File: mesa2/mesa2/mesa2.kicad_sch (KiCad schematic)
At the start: 49 parts, among them J2 Tag-Connect TC2030

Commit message: Record the Rev B design review
The board passes: DRC has no errors, schematic parity is clean, the
outline closes through the Tiny2040 cutout, all 36 footprints still sit
where revb-placement.json puts them, and the silkscreen carries the rev.

Correct the GPIO map in LAYOUT.md, which still claimed the columns ran
GP4 up to GP7. They run GP7 down to GP4 now, reassigned after the
columns paired by finger, and the firmware reads that table.

Assisted-by: Claude:opus-5
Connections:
- net COL_1: now also A1.7 (GP7); no longer A1.4 (GP4)
- net COL_2: now also A1.6 (GP6); no longer A1.5 (GP5)
- net COL_3: now also A1.5 (GP5); no longer A1.6 (GP6)
- net COL_4: now also A1.4 (GP4); no longer A1.7 (GP7)

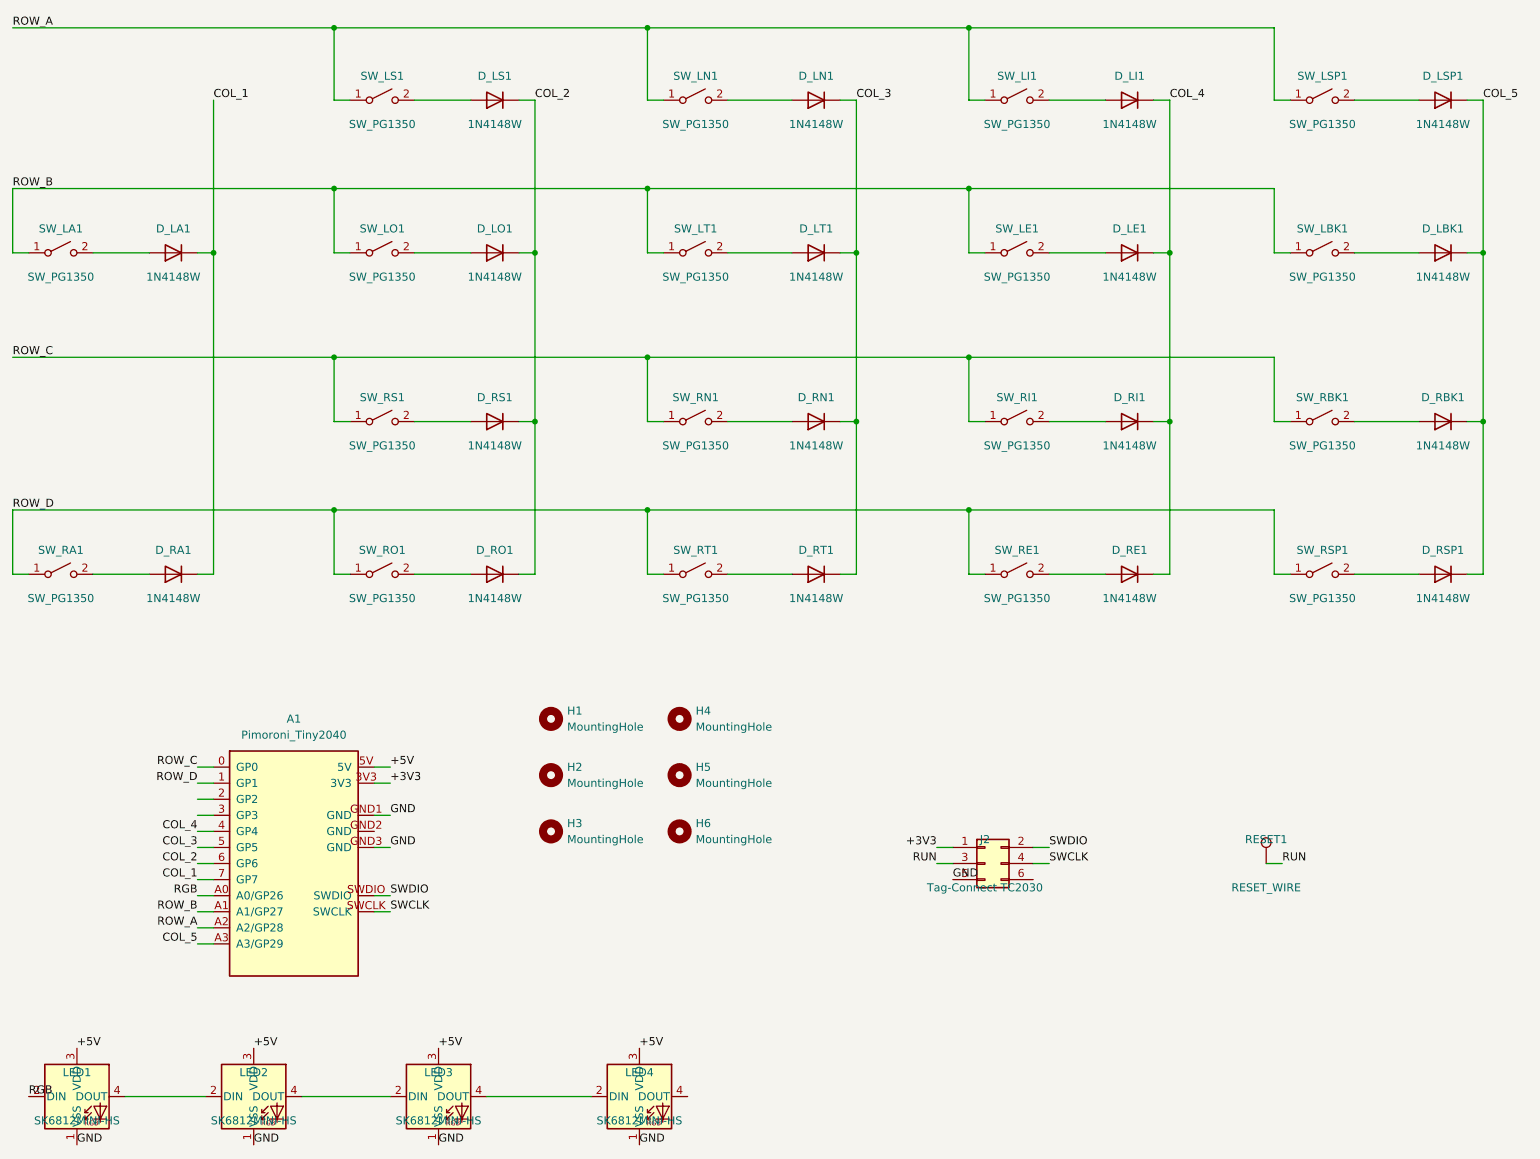
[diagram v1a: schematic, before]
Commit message: Finish mesa2 Rev B
Rev B is complete: 18 keys with the outer pinky gone, the pinky caps
turned to line up with the other fingers, the thumbs on the same 17 mm
pitch as the finger rows, and columns paired by finger so one keymap
serves this board and the Mesa 3 alike.

Design the SK6812 supply fix in, rather than leaving it as the hand
rework Rev A needed. D_RE2 drops the LED rail to ~4.3 V so the RP2040's
3.3 V data clears the 0.7*VDD threshold, JP1 sits open across it as an
escape hatch for a lot that does not need the drop, and C1-C4 decouple
each LED. LAYOUT.md records why, since Mesa 3 inherits this circuit and
the reasoning is not visible in the netlist.

DRC has no errors and schematic parity is clean. ERC gains one benign
entry: +4V5 has no power-output pin driving it, which a PWR_FLAG would
silence.

Assisted-by: Claude:opus-5
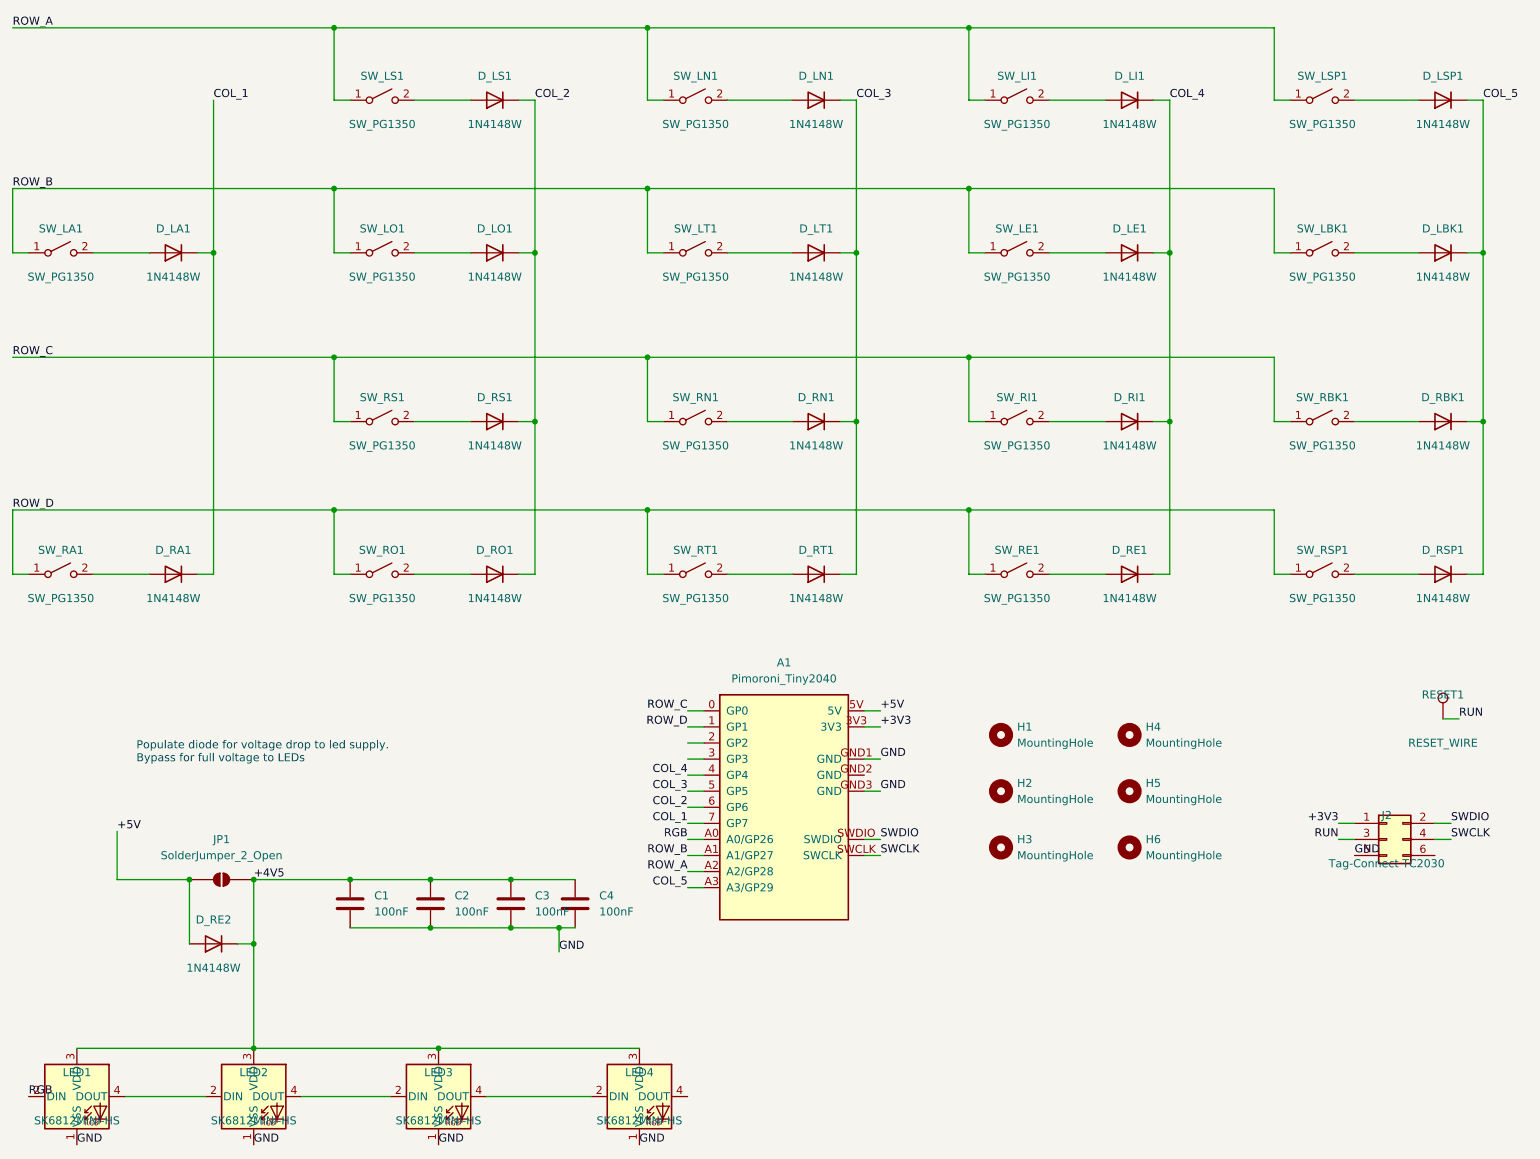
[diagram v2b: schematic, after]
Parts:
- added C1, C2, C3, C4: 100nF, Capacitor_SMD:C_0603_1608Metric_Pad1.08x0.95mm_HandSolder, symbol Device:C
- added D_RE2: 1N4148W, Diode_SMD:D_SOD-123, symbol Device:D
- added JP1: SolderJumper_2_Open, Jumper:SolderJumper-2_P1.3mm_Open_RoundedPad1.0x1.5mm, symbol Jumper:SolderJumper_2_Open
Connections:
- net +5V: now also D_RE2.2 (A), JP1.1 (A); no longer LED1.3 (VDD), LED2.3 (VDD), LED3.3 (VDD), LED4.3 (VDD)
- net GND: now also C1.2, C2.2, C3.2, C4.2
- new net +4V5: C1.1, C2.1, C3.1, C4.1, D_RE2.1 (K), JP1.2 (B), LED1.3 (VDD), LED2.3 (VDD), LED3.3 (VDD), LED4.3 (VDD)
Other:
- note added: "Populate diode for voltage drop to led supply. Bypass for full voltage to LEDs"
- moved on the sheet: A1, H1, H2, H3, H4, H5, H6, J2, RESET1

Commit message: Tidy the Rev B LED supply and power flags
Rename the LED series diode to D1, out of the matrix-diode naming it
first landed in, where it would have sat beside D_RE1 in the BOM and
read like a key diode. Add PWR_FLAGs to +5V and +4V5, which clears the
"input power pin not driven" reports that inserting a diode in a rail
produces. ERC goes from 12 entries to 10; DRC still has no errors and
parity is clean.

Record in LAYOUT.md what still reports and why, all of it inherited from
Rev A: GND has no flag of its own, A1's GND2 sits on no net, and GND1 has
no copper reaching it. Clearing those three is cosmetic, and worth it
only so that a real problem cannot hide in the noise later.

Assisted-by: Claude:opus-5
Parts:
- renumbered D_RE2 to D1
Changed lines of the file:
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@@
 		(color 0 0 0 0)
 	)
+	(junction
+		(at 39.37 157.48)
+		(diameter 0)
+		(color 0 0 0 0)
+	)
 	(wire
 		(pts
@@
 	)
 	(symbol
+		(lib_id "power:PWR_FLAG")
+		(at 76.2 157.48 0)
+		(unit 1)
+		(body_style 1)
+		(exclude_from_sim no)
+		(in_bom yes)
+		(on_board yes)
+		(in_pos_files yes)
+		(dnp no)
+		(fields_autoplaced yes)
+		(property "Reference" "#FLG01"
+			(at 76.2 155.575 0)
+			(hide yes)
+			(show_name no)
+			(do_not_autoplace no)
+			(effects
+				(font
+					(size 1.27 1.27)
+				)
+			)
+		)
+		(property "Value" "PWR_FLAG"
+			(at 76.2 152.4 0)
+			(show_name no)
+			(do_not_autoplace no)
+			(effects
+				(font
+					(size 1.27 1.27)
+				)
+			)
+		)
+		(property "Footprint" ""
+			(at 76.2 157.48 0)
+			(hide yes)
+			(show_name no)
+			(do_not_autoplace no)
+			(effects
+				(font
+					(size 1.27 1.27)
+				)
+			)
+		)
+		(property "Datasheet" ""
+			(at 76.2 157.48 0)
+			(hide yes)
+			(show_name no)
+			(do_not_autoplace no)
+			(effects
+				(font
+					(size 1.27 1.27)
+				)
+			)
+		)
+		(property "Description" "Special symbol for telling ERC where power comes from"
+			(at 76.2 157.48 0)
+			(hide yes)
+			(show_name no)
+			(do_not_autoplace no)
+			(effects
+				(font
+					(size 1.27 1.27)
+				)
+			)
+		)
+		(pin "1"
+		)
+		(instances
+			(project "mesa2"
+				(path "/6762c7a5-6197-445d-9eb4-2a300e3d331b"
+					(reference "#FLG01")
+					(unit 1)
+				)
+			)
+		)
+	)
+	(symbol
 		(lib_id "Switch:SW_SPST")
 		(at 229.87 85.09 0)
@@
 		(in_pos_files yes)
 		(dnp no)
-		(property "Reference" "D_RE2"
+		(property "Reference" "D1"
 			(at 54.61 163.83 0)
 			(show_name no)
@@
 			(project "mesa2"
 				(path "/6762c7a5-6197-445d-9eb4-2a300e3d331b"
-					(reference "D_RE2")
+					(reference "D1")
 					(unit 1)
 				)
@@
 					(unit 1)
 				)
+			)
+		)
+	)
+	(symbol
+		(lib_id "power:PWR_FLAG")
+		(at 39.37 157.48 90)
+		(unit 1)
+		(body_style 1)
+		(exclude_from_sim no)
+		(in_bom yes)
+		(on_board yes)
+		(in_pos_files yes)
+		(dnp no)
+		(fields_autoplaced yes)
+		(property "Reference" "#FLG02"
+			(at 37.465 157.48 0)
+			(hide yes)
+			(show_name no)
+			(do_not_autoplace no)
+			(effects
+				(font
+					(size 1.27 1.27)
+				)
+			)
+		)
+		(property "Value" "PWR_FLAG"
+			(at 35.56 157.4799 90)
+			(show_name no)
+			(do_not_autoplace no)
+			(effects
+				(font
+					(size 1.27 1.27)
+				)
+				(justify left)
+			)
+		)
+		(property "Footprint" ""
+			(at 39.37 157.48 0)
+			(hide yes)
+			(show_name no)
+			(do_not_autoplace no)
+			(effects
+				(font
+					(size 1.27 1.27)
+				)
+			)
+		)
+		(property "Datasheet" ""
+			(at 39.37 157.48 0)
+			(hide yes)
+			(show_name no)
+			(do_not_autoplace no)
+			(effects
+				(font
+					(size 1.27 1.27)
+				)
+			)
+		)
+		(property "Description" "Special symbol for telling ERC where power comes from"
+			(at 39.37 157.48 0)
+			(hide yes)
+			(show_name no)
+			(do_not_autoplace no)
+			(effects
+				(font
+					(size 1.27 1.27)
+				)
+			)
+		)
+		(pin "1"
+		)
+		(instances
+			(project "mesa2"
+				(path "/6762c7a5-6197-445d-9eb4-2a300e3d331b"
+					(reference "#FLG02")
+					(unit 1)
+				)
